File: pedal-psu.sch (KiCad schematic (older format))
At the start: 65 parts, among them J1 Conn_01x01_Male, J2 Conn_01x01_Male, J3 Conn_01x02_Male, J4 Conn_01x02_Male, J5 Conn_01x02_Male, J6 Conn_01x02_Male, T1 Transformer_1P_1S, T2 Transformer_1P_1S, U1 LM7809_TO220, U2 LM324, U4 LM7805_TO220, U5 LM317_3PinPackage

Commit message: Complete schematic, moving on to PCB design.
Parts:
- removed J3, J4, J5, J6: Conn_01x02_Male, Connector_Molex:Molex_KK-254_AE-6410-02A_1x02_P2.54mm_Vertical, symbol Connector:Conn_01x02_Male
- added C15, C19, C20: 100n, Capacitor_SMD:C_1210_3225Metric_Pad1.42x2.65mm_HandSolder, symbol Device:C
- added C16: CP, Capacitor_THT:C_Radial_D10.0mm_H12.5mm_P5.00mm, symbol Device:CP
- added C17, C18: CP, Capacitor_THT:C_Radial_D6.3mm_H5.0mm_P2.50mm, symbol Device:CP
- added D10, D11, D12, D9: 1N4001, Diode_SMD:D_SMA_Handsoldering, symbol Diode:1N4001
- added J3: Power Sockets, Connector_Molex:Molex_KK-254_AE-6410-10A_1x10_P2.54mm_Vertical, symbol Connector:Conn_01x10_Male
- added J4: LCD Display, Connector_Molex:Molex_KK-254_AE-6410-10A_1x10_P2.54mm_Vertical, symbol Connector:Conn_01x10_Male
- added J7: Status LEDS, Connector_Molex:Molex_KK-254_AE-6410-10A_1x10_P2.54mm_Vertical, symbol Connector:Conn_01x10_Male
- added R26: 220, Resistor_SMD:R_0805_2012Metric_Pad1.15x1.40mm_HandSolder, symbol Device:R
- added R30: 100k, Resistor_SMD:R_0805_2012Metric_Pad1.15x1.40mm_HandSolder, symbol Device:R
- added R31, R32, R33, R34, R35, R36, R37, R38: 560, Resistor_SMD:R_0805_2012Metric_Pad1.15x1.40mm_HandSolder, symbol Device:R
- added RV4: 10k, Potentiometer_THT:Potentiometer_Piher_PT-6-V_Vertical, symbol Device:R_POT
- added U3, U6: LM7809_TO220, Package_TO_SOT_THT:TO-220-3_Vertical, symbol Regulator_Linear:LM7809_TO220
- added U7: 74HC595, Package_SO:SOP-16_4.4x10.4mm_P1.27mm, symbol 74xx:74HC595
- T1, T2: footprint Transformer_THT:Transformer_CHK_EI42-5VA_1xSec -> pedal-psu:Transformer_V42AJ
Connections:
- net +5V: now also C15.1, J4.2 (Pin_2), R26.2, R30.1, RV4.3, U7.16 (VCC)
- net +ADJV: now also J3.8 (Pin_8)
- net GND: now also C10.2, C11.2, C12.2, C13.2, C14.2, C9.2, D8.2 (A), RV3.2, RV3.3, U4.2 (GND), C15.2, C16.2, C17.2, C18.2, C19.2, C20.2, D11.2 (A), D12.2 (A), J3.1 (Pin_1), J3.10 (Pin_10), J4.1 (Pin_1), J7.1 (Pin_1), RV4.1, U3.2 (GND), U6.2 (GND), U7.13 (~OE), U7.8 (GND)
- net at C1.1, C2.1, D1.1 (+)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: now also C16.1, D10.1 (K), D9.1 (K), U3.1 (VI), U6.1 (VI)
- net GND_2: now reaches R8.1, U2.5 (+)
- net GND_2: now also J3.5 (Pin_5)
- net GND_1: now reaches R7.1, U2.3 (+)
- net GND_1: now also J3.3 (Pin_3)
- net GND_3: now reaches R9.1, U2.10 (+)
- net GND_3: now also J3.7 (Pin_7)
- net GND_ADJ: now reaches R21.1, U2.12 (+)
- net GND_ADJ: now also J3.9 (Pin_9)
- net LCD7: now reaches A1.10 (D7)
- net LCD7: now also J4.9 (Pin_9)
- net RS: now reaches A1.11 (D8)
- net RS: now also J4.4 (Pin_4)
- net ENABLE: now reaches A1.12 (D9)
- net ENABLE: now also J4.5 (Pin_5)
- net SS: now reaches A1.13 (D10)
- net SS: now also U7.12 (RCLK)
- net MOSI: now reaches A1.14 (D11)
- net MOSI: now also U7.14 (SER)
- net MISO: now reaches A1.15 (D12)
- net SCK: now reaches A1.16 (D13)
- net SCK: now also U7.11 (SRCLK)
- net BUTTON: now reaches A1.5 (D2)
- net BUTTON: now also J7.10 (Pin_10)
- net LCD4: now reaches A1.7 (D4)
- net LCD4: now also J4.6 (Pin_6)
- net LCD5: now reaches A1.8 (D5)
- net LCD5: now also J4.7 (Pin_7)
- net LCD6: now reaches A1.9 (D6)
- net LCD6: now also J4.8 (Pin_8)
- net +9V renamed +9V_1
- net +9V_1: now also J3.2 (Pin_2); no longer R3.1, R5.1
- new net: R32.1, U7.1 (QB)
- new net: R30.2, U7.10 (~SRCLR)
- new net: R31.1, U7.15 (QA)
- new net: R33.1, U7.2 (QC)
- new net: R34.1, U7.3 (QD)
- new net: R35.1, U7.4 (QE)
- new net: R36.1, U7.5 (QF)
- new net: R37.1, U7.6 (QG)
- new net: R38.1, U7.7 (QH)
- new net: J7.2 (Pin_2), R31.2
- new net: J7.3 (Pin_3), R32.2
- new net: J7.4 (Pin_4), R33.2
- new net: J7.5 (Pin_5), R34.2
- new net: J7.6 (Pin_6), R35.2
- new net: J7.7 (Pin_7), R36.2
- new net: J7.8 (Pin_8), R37.2
- new net: J7.9 (Pin_9), R38.2
- new net: J4.10 (Pin_10), R26.1
- new net +9V_2: C17.1, C19.1, D11.1 (K), D9.2 (A), J3.4 (Pin_4), R3.1, U3.3 (VO)
- new net +9V_3: C18.1, C20.1, D10.2 (A), D12.1 (K), J3.6 (Pin_6), R5.1, U6.3 (VO)
- new net VO: J4.3 (Pin_3), RV4.2
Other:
- moved on the sheet: A1, C1, C10, C11, C12, C13, C14, C2, C3, C4, C5, C6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

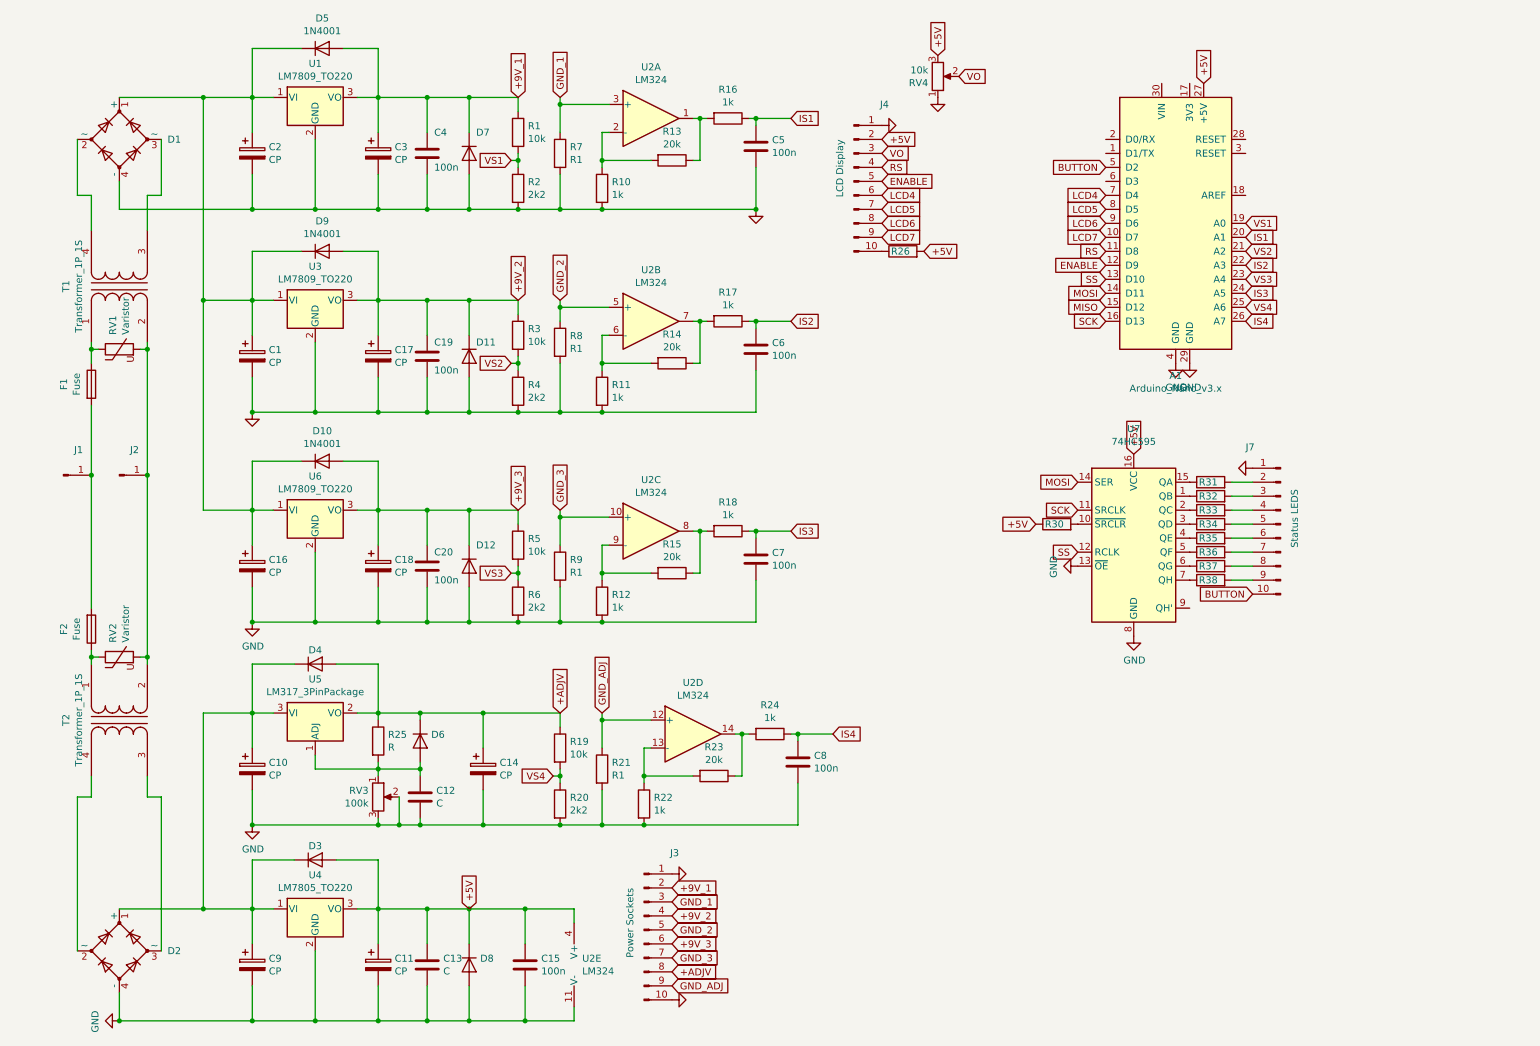
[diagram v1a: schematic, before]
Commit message: Moving Op-Amp into place.
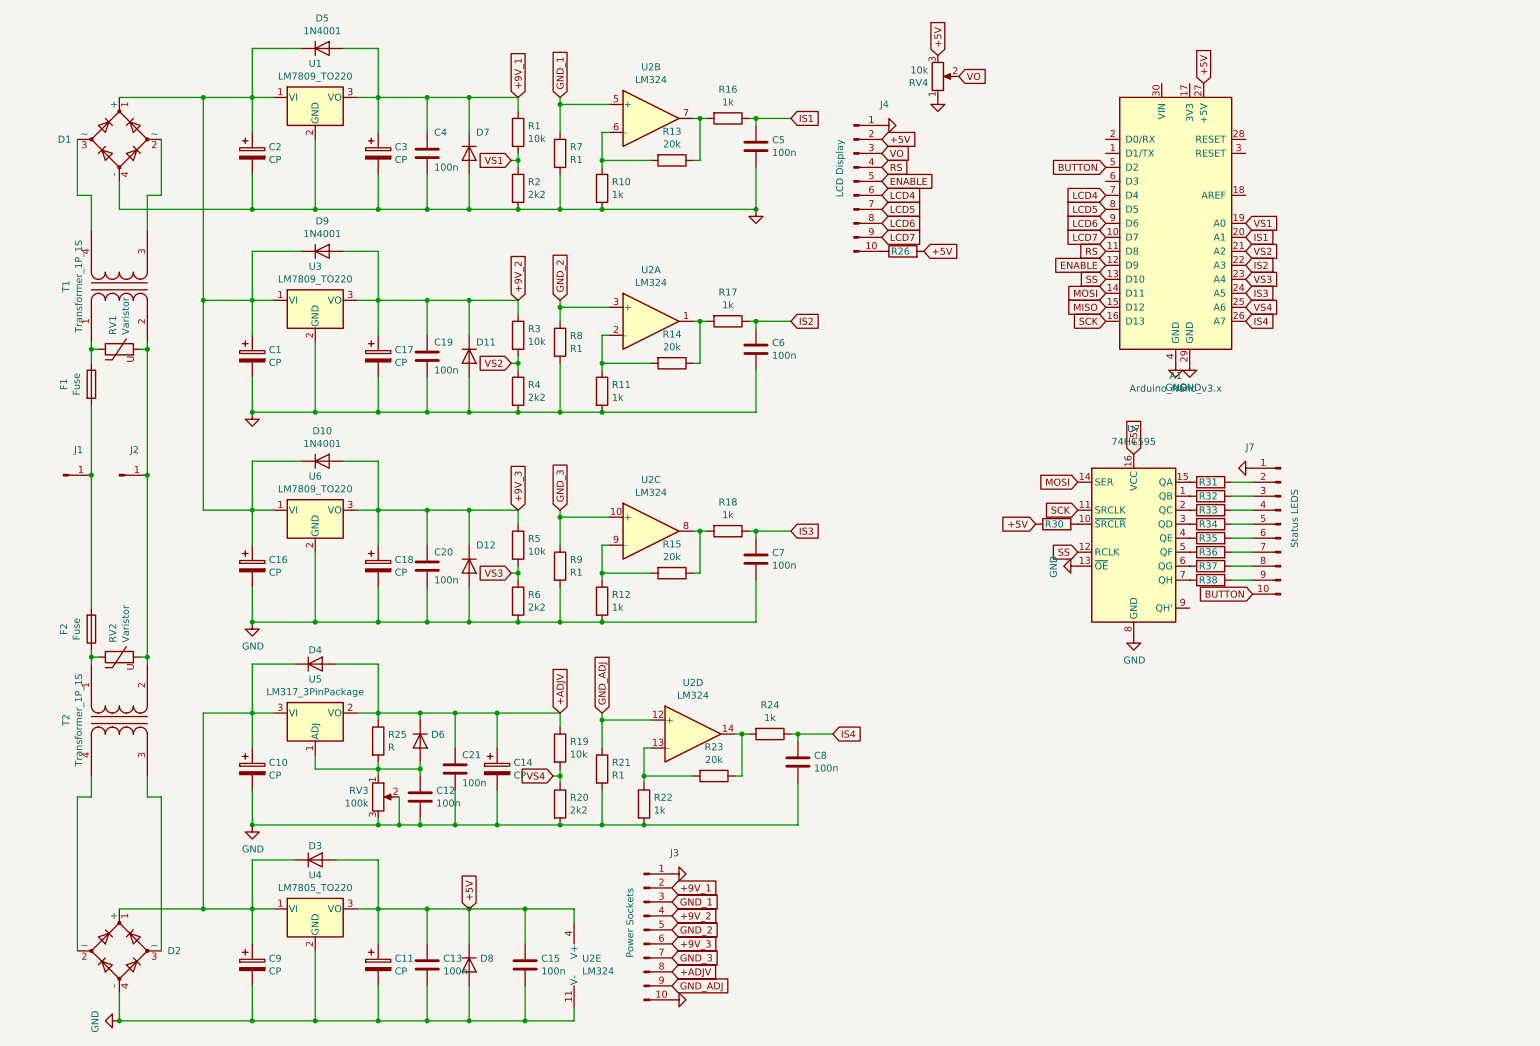
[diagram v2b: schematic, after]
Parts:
- added C21: 100n, Capacitor_SMD:C_1210_3225Metric_Pad1.42x2.65mm_HandSolder, symbol Device:C
- C12, C13: value C -> 100n
- D1, D2: footprint Diode_THT:Diode_Bridge_Vishay_KBL -> PartsStash:Diode_Bridge_TELPOD_GB009_p4mm
- F1, F2: footprint pedal-psu:Fuse-PTF15 -> PartsStash:Fuse-PTF15
- J1, J2: footprint pedal-psu:Blade_3866B.68 -> PartsStash:Blade_3866B.68
- T1, T2: footprint pedal-psu:Transformer_V42AJ -> PartsStash:Transformer_V42AJ
- U1, U3, U4, U5, U6: footprint Package_TO_SOT_THT:TO-220-3_Vertical -> PartsStash:TO220_Vertical_Radiator_L15mm_W10mm
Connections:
- net +ADJV: now also C21.1
- net GND: now also C21.2
- net GND_1: now also U2.5 (+); no longer U2.3 (+)
- net GND_2: now also U2.3 (+); no longer U2.5 (+)
- net at T1.3 (SA): now also D1.2 (~~); no longer D1.3 (~~)
- net at T1.4 (SB): now also D1.3 (~~); no longer D1.2 (~~)
- net at R11.1, R14.2: now also U2.2 (-); no longer U2.6 (-)
- net at R14.1, R17.2: now also U2.1; no longer U2.7
- net at R13.1, R16.2: now also U2.7; no longer U2.1
- net at R10.1, R13.2: now also U2.6 (-); no longer U2.2 (-)
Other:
- moved on the sheet: C14, U2A, U2B
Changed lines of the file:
@@
 F 0 "T1" H 1150 2781 50  0000 C CNN
 F 1 "Transformer_1P_1S" H 1150 2690 50  0000 C CNN
-F 2 "pedal-psu:Transformer_V42AJ" H 1150 2400 50  0001 C CNN
+F 2 "PartsStash:Transformer_V42AJ" H 1150 2400 50  0001 C CNN
 F 3 "~" H 1150 2400 50  0001 C CNN
 	1    1150 2400
@@
 F 0 "T2" H 1150 5881 50  0000 C CNN
 F 1 "Transformer_1P_1S" H 1150 5790 50  0000 C CNN
-F 2 "pedal-psu:Transformer_V42AJ" H 1150 5500 50  0001 C CNN
+F 2 "PartsStash:Transformer_V42AJ" H 1150 5500 50  0001 C CNN
 F 3 "~" H 1150 5500 50  0001 C CNN
 	1    1150 5500
@@
 F 0 "F1" V 753 3100 50  0000 C CNN
 F 1 "Fuse" V 844 3100 50  0000 C CNN
-F 2 "pedal-psu:Fuse-PTF15" V 880 3100 50  0001 C CNN
+F 2 "PartsStash:Fuse-PTF15" V 880 3100 50  0001 C CNN
 F 3 "~" H 950 3100 50  0001 C CNN
 	1    950  3100
@@
 F 0 "F2" V 753 4850 50  0000 C CNN
 F 1 "Fuse" V 844 4850 50  0000 C CNN
-F 2 "pedal-psu:Fuse-PTF15" V 880 4850 50  0001 C CNN
+F 2 "PartsStash:Fuse-PTF15" V 880 4850 50  0001 C CNN
 F 3 "~" H 950 4850 50  0001 C CNN
 	1    950  4850
@@
 F 0 "J1" H 858 3931 50  0000 C CNN
 F 1 "Conn_01x01_Male" H 750 3850 50  0001 C CNN
-F 2 "pedal-psu:Blade_3866B.68" H 750 3750 50  0001 C CNN
+F 2 "PartsStash:Blade_3866B.68" H 750 3750 50  0001 C CNN
 F 3 "~" H 750 3750 50  0001 C CNN
 	1    750  3750
@@
 F 0 "J2" H 1258 3931 50  0000 C CNN
 F 1 "Conn_01x01_Male" H 1258 3840 50  0001 C CNN
-F 2 "pedal-psu:Blade_3866B.68" H 1150 3750 50  0001 C CNN
+F 2 "PartsStash:Blade_3866B.68" H 1150 3750 50  0001 C CNN
 F 3 "~" H 1150 3750 50  0001 C CNN
 	1    1150 3750
@@
 F 0 "D1" V 1150 1006 50  0000 R CNN
 F 1 "D_Bridge_+AA-" V 1105 1006 50  0001 R CNN
-F 2 "Diode_THT:Diode_Bridge_Vishay_KBL" H 1150 1350 50  0001 C CNN
+F 2 "PartsStash:Diode_Bridge_TELPOD_GB009_p4mm" H 1150 1350 50  0001 C CNN
 F 3 "~" H 1150 1350 50  0001 C CNN
 	1    1150 1350
-	0    -1   -1   0
+	0    1    -1   0
 $EndComp
 Wire Wire Line
@@
 F 0 "U1" H 2550 1292 50  0000 C CNN
 F 1 "LM7809_TO220" H 2550 1201 50  0000 C CNN
-F 2 "Package_TO_SOT_THT:TO-220-3_Vertical" H 2550 1275 50  0001 C CIN
+F 2 "PartsStash:TO220_Vertical_Radiator_L15mm_W10mm" H 2550 1275 50  0001 C CIN
 F 3 "http://www.fairchildsemi.com/ds/LM/LM7805.pdf" H 2550 1000 50  0001 C CNN
 	1    2550 1050
@@
 F 0 "D2" V 1150 6806 50  0000 R CNN
 F 1 "D_Bridge_+AA-" V 1105 6806 50  0001 R CNN
-F 2 "Diode_THT:Diode_Bridge_Vishay_KBL" H 1150 7150 50  0001 C CNN
+F 2 "PartsStash:Diode_Bridge_TELPOD_GB009_p4mm" H 1150 7150 50  0001 C CNN
 F 3 "~" H 1150 7150 50  0001 C CNN
 	1    1150 7150
@@
 L Amplifier_Operational:LM324 U2
 U 2 1 5C1EEF4A
-P 4950 2650
-F 0 "U2" H 4950 3017 50  0000 C CNN
-F 1 "LM324" H 4950 2926 50  0000 C CNN
-F 2 "Package_SO:SOIC-14_3.9x8.7mm_P1.27mm" H 4900 2750 50  0001 C CNN
-F 3 "http://www.ti.com/lit/ds/symlink/lm2902-n.pdf" H 5000 2850 50  0001 C CNN
-	2    4950 2650
+P 4950 1200
+F 0 "U2" H 4950 1567 50  0000 C CNN
+F 1 "LM324" H 4950 1476 50  0000 C CNN
+F 2 "Package_SO:SOIC-14_3.9x8.7mm_P1.27mm" H 4900 1300 50  0001 C CNN
+F 3 "http://www.ti.com/lit/ds/symlink/lm2902-n.pdf" H 5000 1400 50  0001 C CNN
+	2    4950 1200
 	1    0    0    -1
 $EndComp
@@
 L Amplifier_Operational:LM324 U2
 U 1 1 5C24BF08
-P 4950 1200
-F 0 "U2" H 4950 1567 50  0000 C CNN
-F 1 "LM324" H 4950 1476 50  0000 C CNN
-F 2 "Package_SO:SOIC-14_3.9x8.7mm_P1.27mm" H 4900 1300 50  0001 C CNN
-F 3 "http://www.ti.com/lit/ds/symlink/lm2902-n.pdf" H 5000 1400 50  0001 C CNN
-	1    4950 1200
+P 4950 2650
+F 0 "U2" H 4950 3017 50  0000 C CNN
+F 1 "LM324" H 4950 2926 50  0000 C CNN
+F 2 "Package_SO:SOIC-14_3.9x8.7mm_P1.27mm" H 4900 2750 50  0001 C CNN
+F 3 "http://www.ti.com/lit/ds/symlink/lm2902-n.pdf" H 5000 2850 50  0001 C CNN
+	1    4950 2650
 	1    0    0    -1
 $EndComp
@@
 P 3350 7250
 F 0 "C13" H 3465 7296 50  0000 L CNN
-F 1 "C" H 3465 7205 50  0000 L CNN
+F 1 "100n" H 3465 7205 50  0000 L CNN
 F 2 "Capacitor_SMD:C_1210_3225Metric_Pad1.42x2.65mm_HandSolder" H 3388 7100 50  0001 C CNN
 F 3 "~" H 3350 7250 50  0001 C CNN
@@
 F 0 "U4" H 2550 7092 50  0000 C CNN
 F 1 "LM7805_TO220" H 2550 7001 50  0000 C CNN
-F 2 "Package_TO_SOT_THT:TO-220-3_Vertical" H 2550 7075 50  0001 C CIN
+F 2 "PartsStash:TO220_Vertical_Radiator_L15mm_W10mm" H 2550 7075 50  0001 C CIN
 F 3 "http://www.fairchildsemi.com/ds/LM/LM7805.pdf" H 2550 6800 50  0001 C CNN
 	1    2550 6850
@@
 F 0 "U5" H 2550 5692 50  0000 C CNN
 F 1 "LM317_3PinPackage" H 2550 5601 50  0000 C CNN
-F 2 "Package_TO_SOT_THT:TO-220-3_Vertical" H 2550 5700 50  0001 C CIN
+F 2 "PartsStash:TO220_Vertical_Radiator_L15mm_W10mm" H 2550 5700 50  0001 C CIN
 F 3 "http://www.ti.com/lit/ds/symlink/lm317.pdf" H 2550 5450 50  0001 C CNN
 	1    2550 5450
@@
 Connection ~ 3300 5450
 Wire Wire Line
-	3300 5450 3750 5450
+	3300 5450 3550 5450
 Wire Wire Line
 	3000 5800 3000 5850
@@
 P 3300 6050
 F 0 "C12" H 3415 6096 50  0000 L CNN
-F 1 "C" H 3415 6005 50  0000 L CNN
+F 1 "100n" H 3415 6005 50  0000 L CNN
 F 2 "Capacitor_SMD:C_1210_3225Metric_Pad1.42x2.65mm_HandSolder" H 3338 5900 50  0001 C CNN
 F 3 "~" H 3300 6050 50  0001 C CNN
@@
 L Device:CP C14
 U 1 1 5C640AC4
-P 3750 5850
-F 0 "C14" H 3868 5896 50  0000 L CNN
-F 1 "CP" H 3868 5805 50  0000 L CNN
-F 2 "Capacitor_THT:C_Radial_D6.3mm_H5.0mm_P2.50mm" H 3788 5700 50  0001 C CNN
-F 3 "~" H 3750 5850 50  0001 C CNN
-	1    3750 5850
-	1    0    0    -1
-$EndComp
-Wire Wire Line
-	3750 5450 3750 5700
-Wire Wire Line
-	3750 6000 3750 6250
-Wire Wire Line
-	3750 6250 3300 6250
+P 3850 5850
+F 0 "C14" H 3968 5896 50  0000 L CNN
+F 1 "CP" H 3968 5805 50  0000 L CNN
+F 2 "Capacitor_THT:C_Radial_D6.3mm_H5.0mm_P2.50mm" H 3888 5700 50  0001 C CNN
+F 3 "~" H 3850 5850 50  0001 C CNN
+	1    3850 5850
+	1    0    0    -1
+$EndComp
+Wire Wire Line
+	3850 5450 3850 5700
+Wire Wire Line
+	3850 6000 3850 6250
+Wire Wire Line
+	3850 6250 3550 6250
 Connection ~ 3300 6250
 $Comp
@@
 	3150 6250 3300 6250
 Wire Wire Line
-	4300 5450 3750 5450
-Connection ~ 3750 5450
+	4300 5450 3850 5450
+Connection ~ 3850 5450
 Text GLabel 3650 6850 1    50   Input ~ 0
 +5V
@@
 F 0 "U3" H 2550 2742 50  0000 C CNN
 F 1 "LM7809_TO220" H 2550 2651 50  0000 C CNN
-F 2 "Package_TO_SOT_THT:TO-220-3_Vertical" H 2550 2725 50  0001 C CIN
+F 2 "PartsStash:TO220_Vertical_Radiator_L15mm_W10mm" H 2550 2725 50  0001 C CIN
 F 3 "http://www.fairchildsemi.com/ds/LM/LM7805.pdf" H 2550 2450 50  0001 C CNN
 	1    2550 2500
@@
 F 0 "U6" H 2550 4242 50  0000 C CNN
 F 1 "LM7809_TO220" H 2550 4151 50  0000 C CNN
-F 2 "Package_TO_SOT_THT:TO-220-3_Vertical" H 2550 4225 50  0001 C CIN
+F 2 "PartsStash:TO220_Vertical_Radiator_L15mm_W10mm" H 2550 4225 50  0001 C CIN
 F 3 "http://www.fairchildsemi.com/ds/LM/LM7805.pdf" H 2550 3950 50  0001 C CNN
 	1    2550 4000
@@
 Connection ~ 3000 6250
 Wire Wire Line
-	4300 6250 3750 6250
+	4300 6250 3850 6250
 Connection ~ 4300 6250
-Connection ~ 3750 6250
+Connection ~ 3850 6250
 Connection ~ 2100 6250
 Wire Wire Line
@@
 Text GLabel 9250 4600 0    50   Input ~ 0
 BUTTON
+$Comp
+L Device:C C21
+U 1 1 5C3C7E38
+P 3550 5850
+F 0 "C21" H 3600 5950 50  0000 L CNN
+F 1 "100n" H 3600 5750 50  0000 L CNN
+F 2 "Capacitor_SMD:C_1210_3225Metric_Pad1.42x2.65mm_HandSolder" H 3588 5700 50  0001 C CNN
+F 3 "~" H 3550 5850 50  0001 C CNN
+	1    3550 5850
+	1    0    0    -1
+$EndComp
+Wire Wire Line
+	3550 5700 3550 5450
+Connection ~ 3550 5450
+Wire Wire Line
+	3550 5450 3850 5450
+Wire Wire Line
+	3550 6000 3550 6250
+Connection ~ 3550 6250
+Wire Wire Line
+	3550 6250 3300 6250
 $EndSCHEMATC
